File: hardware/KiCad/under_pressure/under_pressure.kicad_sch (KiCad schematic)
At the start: 30 parts, among them J1 input, J3 output, U1 TL072, U3 TL072

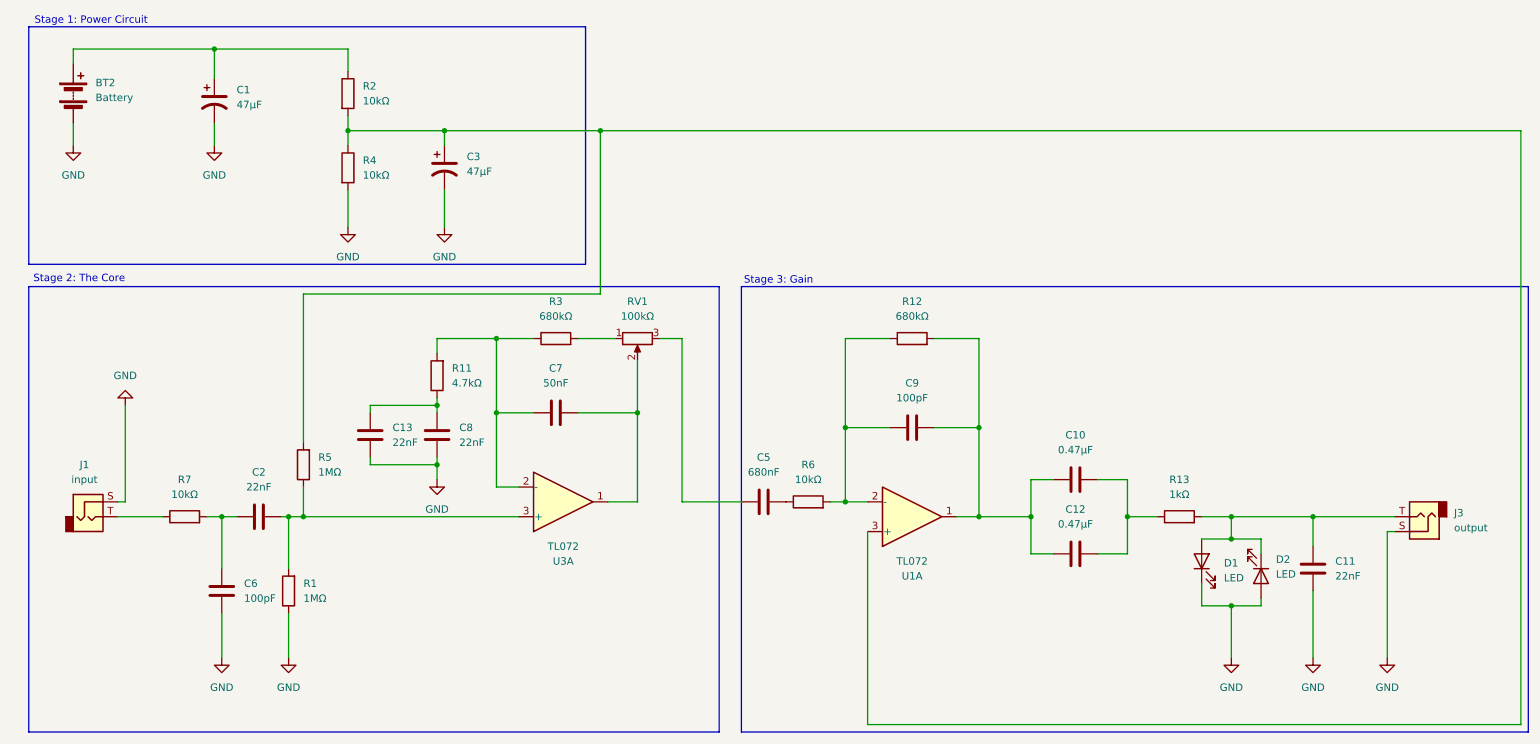
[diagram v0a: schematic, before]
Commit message: cableado + esquematico arreglado
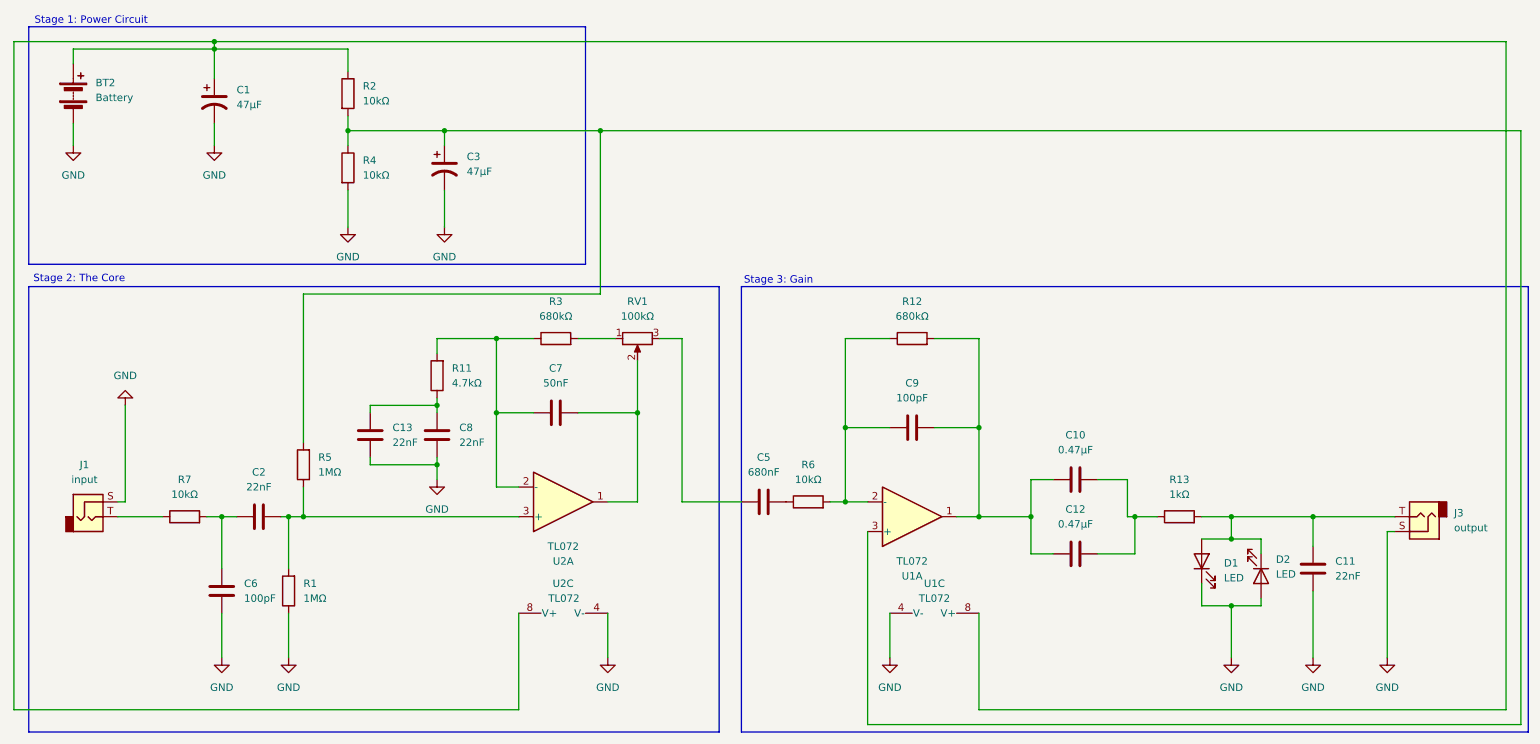
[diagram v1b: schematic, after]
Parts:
- added unit 3 of U1
- added unit 3 of U2
- renumbered U3 to U2
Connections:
- net GND: now also U1.4 (V-), U2.4 (V-)
- net at BT2.1 (+), C1.1, R2.1: now also U1.8 (V+), U2.8 (V+)

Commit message: gerbers
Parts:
- R8: renamed from R3; value 680kΩ -> 2.2kΩ
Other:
- title: Distortion Pedal v1 -> Under Pressure
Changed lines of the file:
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@@
 	(paper "A4")
 	(title_block
-		(title "Distortion Pedal v1")
+		(title "Under Pressure")
 		(date "2026-07-04")
 		(rev "07/04/2026")
@@
 		(dnp no)
 		(fields_autoplaced yes)
-		(property "Reference" "R3"
+		(property "Reference" "R8"
 			(at 110.49 72.39 90)
 			(effects
@@
 			)
 		)
-		(property "Value" "680kΩ"
+		(property "Value" "2.2kΩ"
 			(at 110.49 74.93 90)
 			(effects
@@
 			(project "pedal"
 				(path "/3b4e74c5-522c-48e7-8ef3-cd629b916801"
-					(reference "R3")
+					(reference "R8")
 					(unit 1)
 				)
